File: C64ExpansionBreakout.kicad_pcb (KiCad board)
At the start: 2 copper layers, 99.1 x 90 mm, 6 parts, among them J1 Power, J2 GND, J3 Breakout, SW1 Reset, U1 C64-Exp-Port

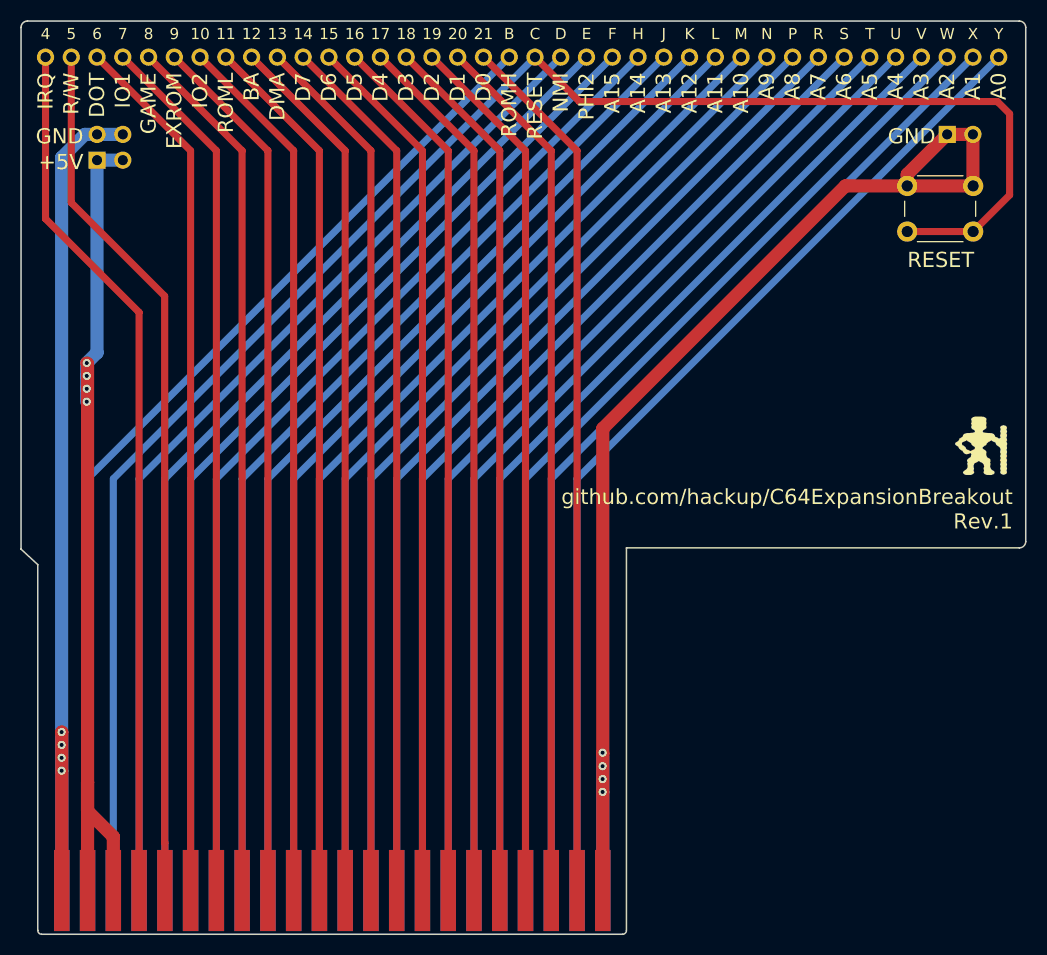
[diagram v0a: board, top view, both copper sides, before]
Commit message: Added 27C512 / 27C020 Eprom socket.
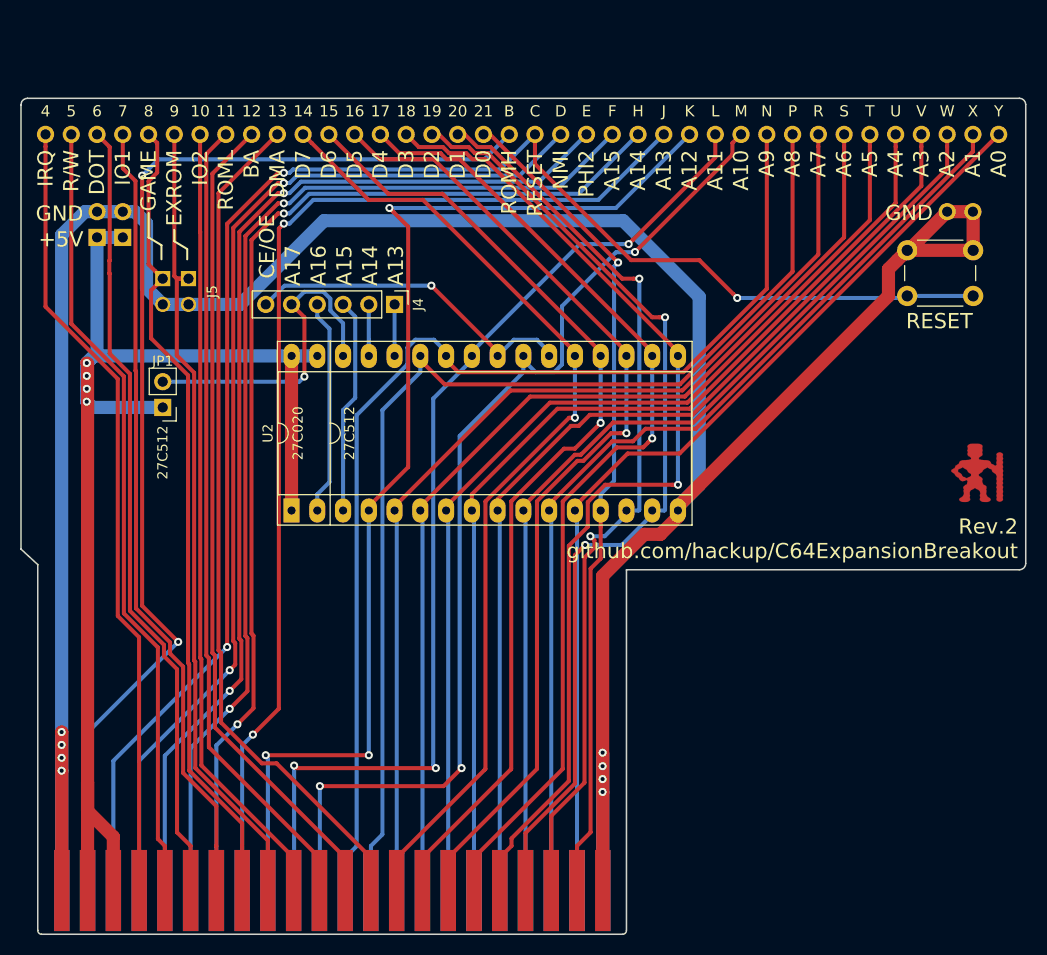
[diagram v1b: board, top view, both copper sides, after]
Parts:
- added J4: Other, Socket_Strips:Socket_Strip_Straight_1x06_Pitch2.54mm, F.Cu at (135.4, 79.0)
- added J5: Config, Pin_Headers:Pin_Header_Straight_2x02_Pitch2.54mm, F.Cu at (115.1, 76.5)
- added JP1: 27c512, Pin_Headers:Pin_Header_Straight_1x02_Pitch2.54mm, F.Cu at (112.5, 89.2)
- added U2: 27C512, Housings_DIP:DIP-32_W15.24mm_Socket_LongPads, F.Cu at (125.2, 99.3)
- moved J1 7.62 mm to (106.0, 72.4)
- moved J2 7.62 mm to (189.9, 69.8)
- moved J3 7.62 mm to (101.0, 62.2)
- moved SW1 6.35 mm to (185.9, 73.7)
- moved G*** 2.69 mm to (192.9, 95.5)
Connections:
- net 5V renamed +5V
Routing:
- net GND: track 214.8 -> 288.5 mm
- net +5V: track 90.5 -> 128.9 mm
- net /CE: track 0.00 -> 33.4 mm, vias 0 -> 1
- net /OA17: track 0.00 -> 32.6 mm, vias 0 -> 1
- net /OA15: track 0.00 -> 21.3 mm
- net /OA16: track 0.00 -> 21.3 mm
- net D3: track 86.0 -> 100.3 mm, vias 0 -> 1
- net ROMH: track 99.4 -> 113.5 mm, vias 0 -> 2
- net A12: track 99.4 -> 112.5 mm, vias 0 -> 3
- net A9: track 99.4 -> 112.3 mm
- net RESET: track 168.1 -> 156.1 mm, vias 0 -> 3
- net D4: track 86.0 -> 97.6 mm, vias 0 -> 1
- net A8: track 99.4 -> 111.0 mm
- net D5: track 86.0 -> 97.3 mm, vias 0 -> 1
- net D6: track 86.0 -> 96.7 mm, vias 0 -> 1
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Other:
- board size 99.1 x 90 mm -> 99.1 x 82.4 mm
- net class Default: trace_width 0.7 -> 0.4
- board text added: "27C020"
- board text added: "27C512"
- board text added: "A16"
- board text added: "A17"
- board text added: "CE/OE"
- board text added: "Rev.2 github.com/hackup/C64ExpansionBreakout"
- board text removed: "github.com/hackup/C64ExpansionBreakout Rev.1"

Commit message: Finalizing revision 2.
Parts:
- added C1: 100n, Capacitors_THT:C_Disc_D4.3mm_W1.9mm_P5.00mm, F.Cu at (121.9, 99.3)
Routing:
- net GND: track 288.5 -> 308.5 mm
- net +5V: track 128.9 -> 132.2 mm
- net GAME: track 80.0 -> 80.7 mm
